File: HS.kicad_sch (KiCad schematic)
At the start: 6 parts, among them IC1 BTS4175SGA

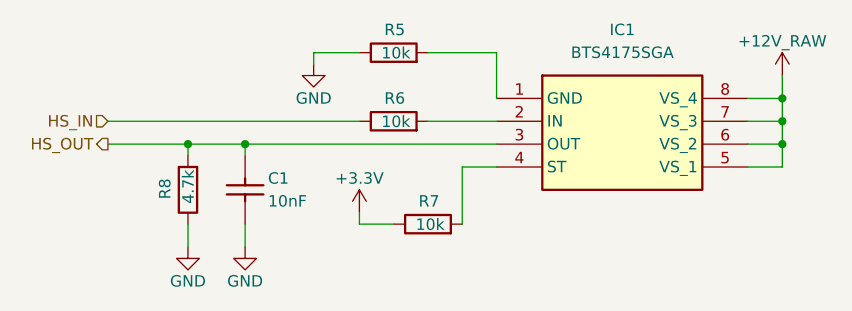
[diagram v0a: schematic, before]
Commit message: Rev A - New Bom-Remplace, fix HS resistors
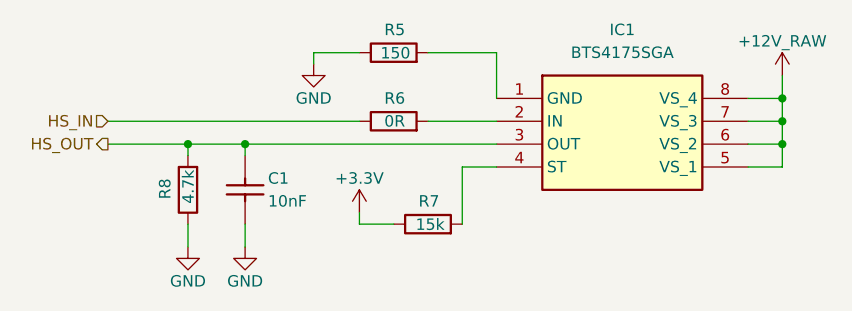
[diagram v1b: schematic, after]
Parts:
- R5: value 10k -> 150; LCSC C25744 -> C325755
- R6: value 10k -> 0R; LCSC C25744 -> C2770782
- R7: value 10k -> 15k; LCSC C25744 -> C881094
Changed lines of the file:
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@@
       (effects (font (size 1.27 1.27)) (justify left))
     )
-    (property "Value" "10k" (at 98.3742 72.4408 90)
+    (property "Value" "15k" (at 98.3742 72.4408 90)
       (effects (font (face "KiCad Font") (size 1.27 1.27)) (justify left))
     )
@@
       (effects (font (size 1.27 1.27)) hide)
     )
-    (property "LCSC" "C25744" (at 96.52 72.39 0)
+    (property "LCSC" "C881094" (at 96.52 72.39 0)
       (effects (font (size 1.27 1.27)) hide)
     )
@@
       (effects (font (size 1.27 1.27)) (justify left))
     )
-    (property "Value" "10k" (at 94.5642 61.0108 90)
+    (property "Value" "0R" (at 93.98 60.96 90)
       (effects (font (face "KiCad Font") (size 1.27 1.27)) (justify left))
     )
@@
       (effects (font (size 1.27 1.27)) hide)
     )
-    (property "LCSC" "C25744" (at 92.71 60.96 0)
+    (property "LCSC" "C2770782" (at 92.71 60.96 0)
       (effects (font (size 1.27 1.27)) hide)
     )
@@
       (effects (font (size 1.27 1.27)) (justify left))
     )
-    (property "Value" "10k" (at 94.5642 53.3908 90)
+    (property "Value" "150" (at 94.5642 53.3908 90)
       (effects (font (face "KiCad Font") (size 1.27 1.27)) (justify left))
     )
@@
       (effects (font (size 1.27 1.27)) hide)
     )
-    (property "LCSC" "C25744" (at 92.71 53.34 0)
+    (property "LCSC" "C325755" (at 92.71 53.34 0)
       (effects (font (size 1.27 1.27)) hide)
     )
